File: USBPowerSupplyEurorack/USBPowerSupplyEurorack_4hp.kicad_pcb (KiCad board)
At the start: 2 copper layers, 19.9 x 110 mm, 36 parts, among them J1 1734366-1, J2 95278-501A10LF, Q1 Q_PMOS_GSD

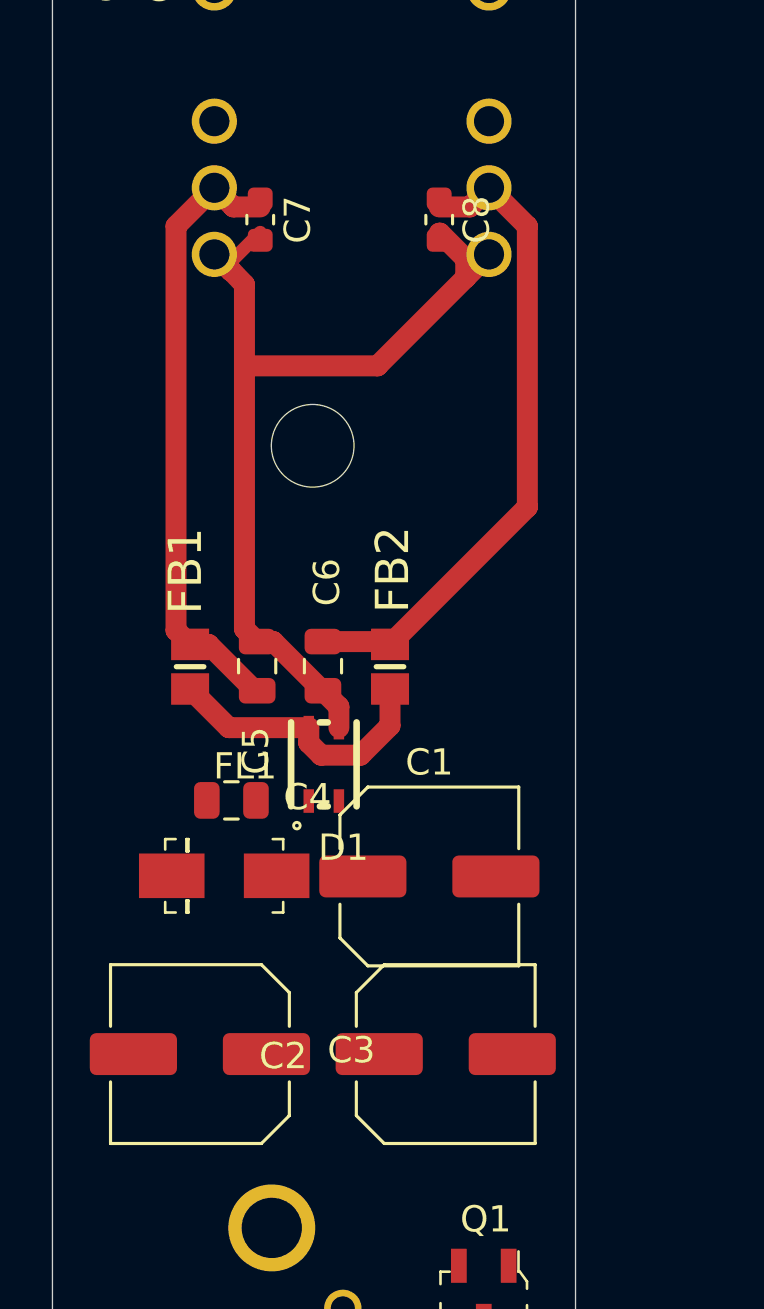
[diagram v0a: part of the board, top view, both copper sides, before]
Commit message: updated components and footprints
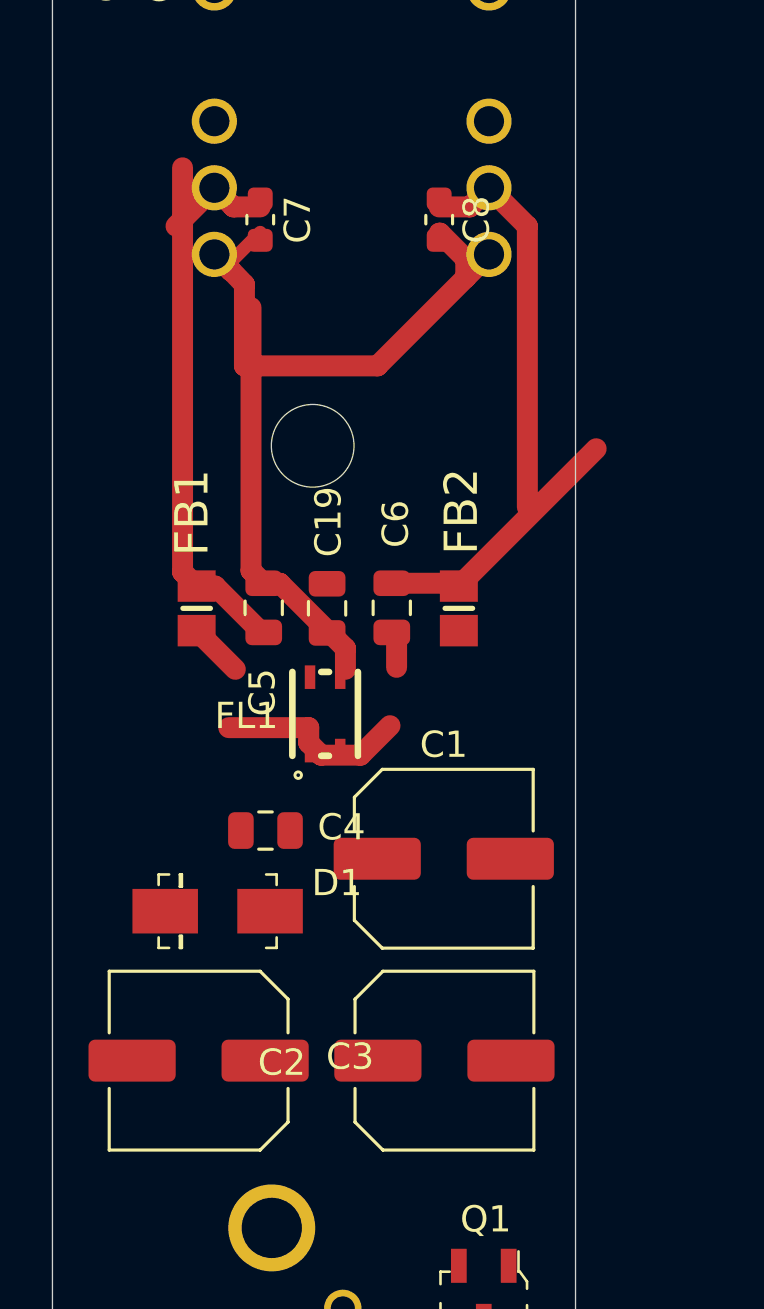
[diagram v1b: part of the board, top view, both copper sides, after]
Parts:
- added C19: 10uF, Capacitor_SMD:C_0805_2012Metric, F.Cu at (140.0, 118.8)
- moved C6 3.44 mm to (142.5, 118.7)
- moved FB2 3.44 mm to (145.1, 118.8)
- moved C5 2.24 mm to (137.6, 118.7)
- moved FB1 2.24 mm to (135.1, 118.8)
- moved FL1 1.93 mm to (139.9, 122.8)
- moved C4 1.74 mm to (137.7, 127.2)
- moved D1 1.37 mm to (135.8, 130.3)
- moved C1 0.87 mm to (144.5, 128.3)
- moved C2 0.25 mm to (144.5, 136.0)
- moved C3 0.25 mm to (135.1, 136.0)
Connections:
- FL1 pad 3: -Vin1 -> Net-(C19-Pad1)
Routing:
- net -Vin1: track 35.6 -> 37.0 mm
- net Net-(FB1-Pad2): track 10.9 -> 9.48 mm

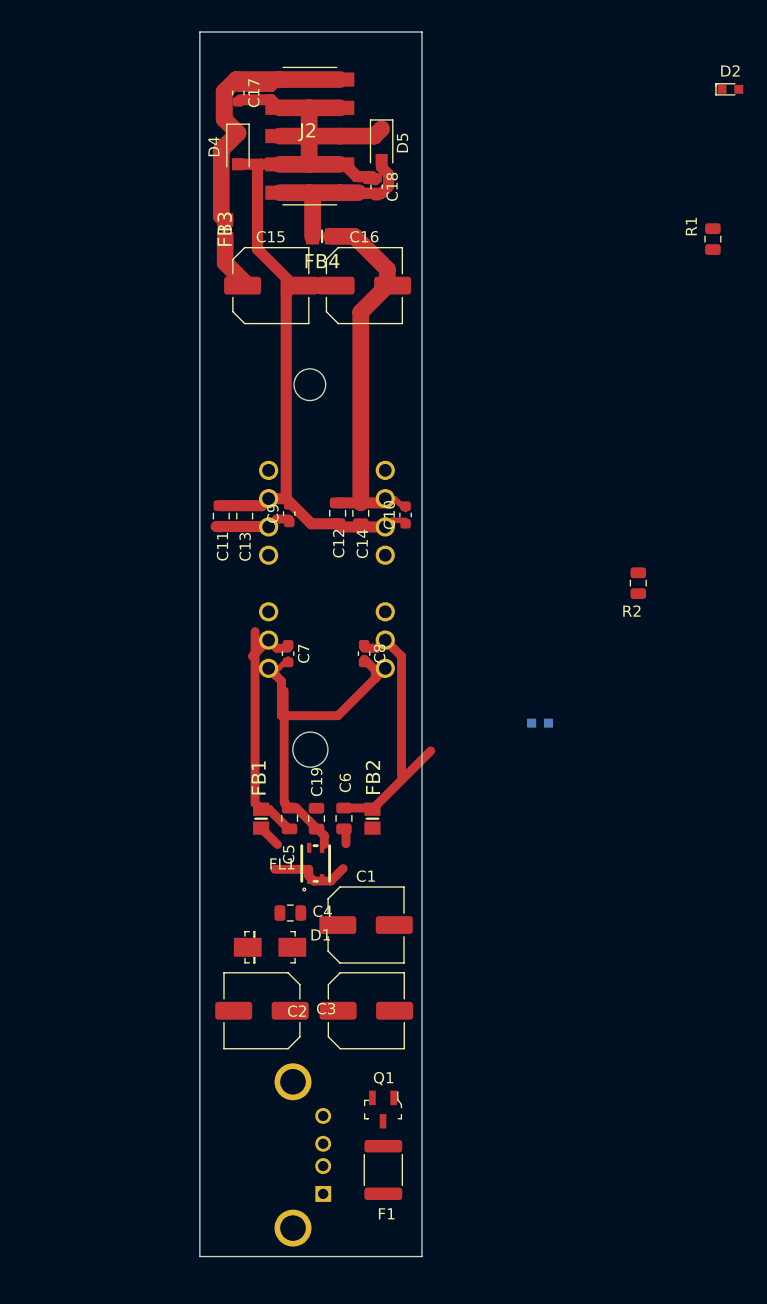
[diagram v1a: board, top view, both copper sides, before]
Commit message: moved holes for panel, updated power plug
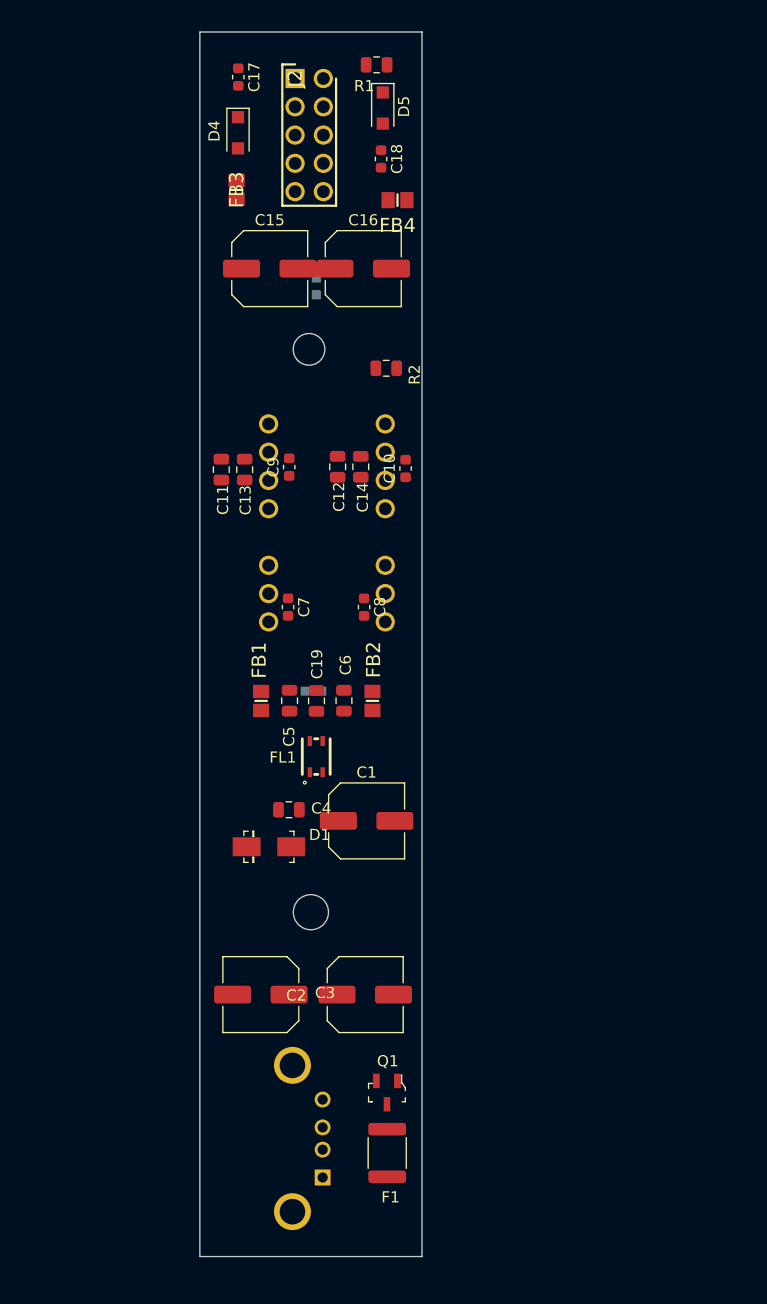
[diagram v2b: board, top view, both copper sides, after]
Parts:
- D2: moved to B.Cu
- J2: value 95278-501A10LF -> 10129381-910001BLF; footprint 95278-501A10LF:95278501A10LF -> HDRV10W67P254_2X5_1270X483X858P
- moved D2 41.2 mm to (140.0, 71.0), turned to 270 degrees
- moved R1 34.0 mm to (145.4, 51.0), turned to 180 degrees
- moved R2 29.7 mm to (146.3, 78.3), turned to 180 degrees
- moved D3 20.6 mm to (139.8, 107.3)
- moved C19 10.6 mm to (140.0, 108.2)
- moved C5 10.6 mm to (137.6, 108.2)
- moved C6 10.6 mm to (142.5, 108.2)
- moved FB1 10.6 mm to (135.1, 108.2)
- moved FB2 10.6 mm to (145.1, 108.2)
- moved FL1 9.60 mm to (140.0, 113.2)
- moved C1 9.35 mm to (144.5, 119.0)
- moved C4 9.28 mm to (137.6, 118.0)
- moved D1 9.03 mm to (135.8, 121.3)
- moved FB4 7.51 mm to (147.3, 63.2)
- moved J2 5.34 mm to (138.1, 52.3)
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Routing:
- net 0V: track 99.2 -> 0.00 mm
- net -Vin1: track 37.0 -> 0.00 mm
- net -12V: track 34.9 -> 0.00 mm
- net Net-(C17-Pad1): track 32.6 -> 0.00 mm
- net +Vin2: track 25.0 -> 0.00 mm
- net +Vin1: track 23.6 -> 0.00 mm
- net Net-(C18-Pad2): track 18.6 -> 0.00 mm
- net +12V: track 12.2 -> 0.00 mm
- net Net-(FB1-Pad2): track 9.48 -> 0.00 mm
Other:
- outline, holes or cut-outs redrawn

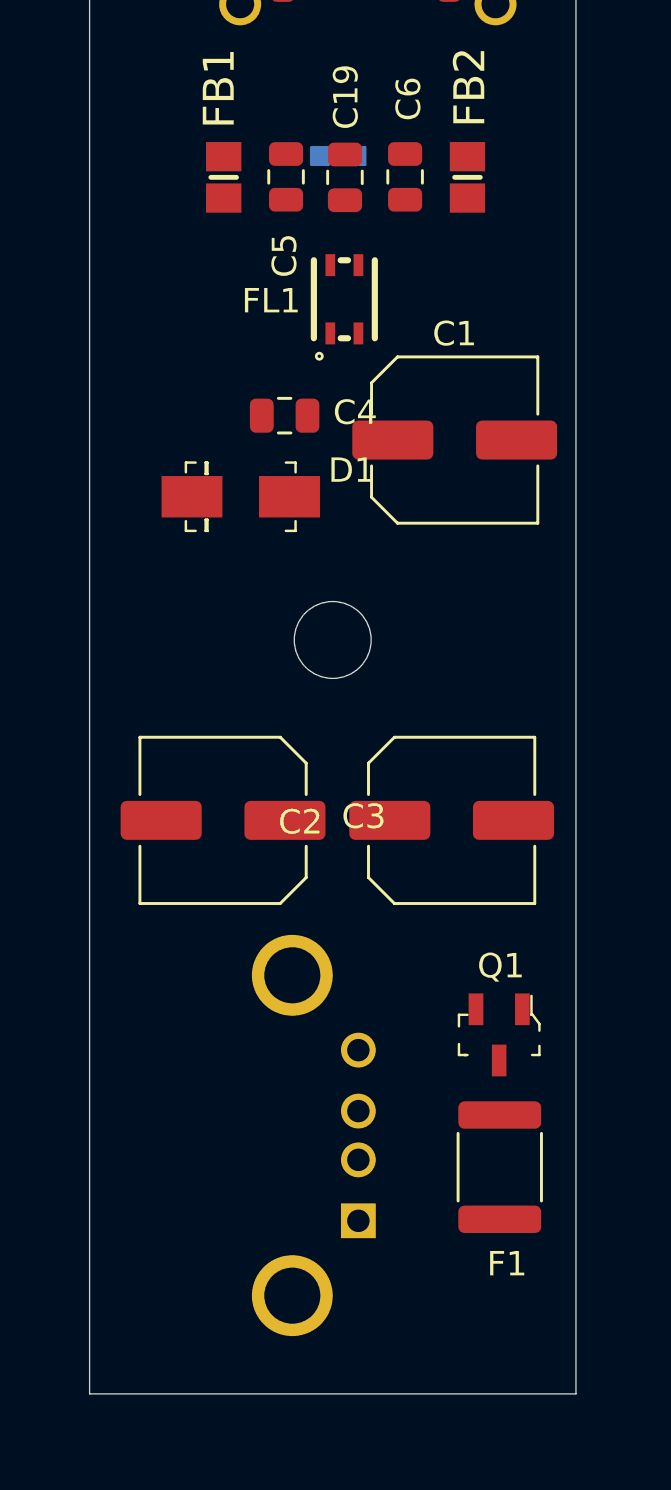
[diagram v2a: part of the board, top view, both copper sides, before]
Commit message: working on the routing, making copper pours
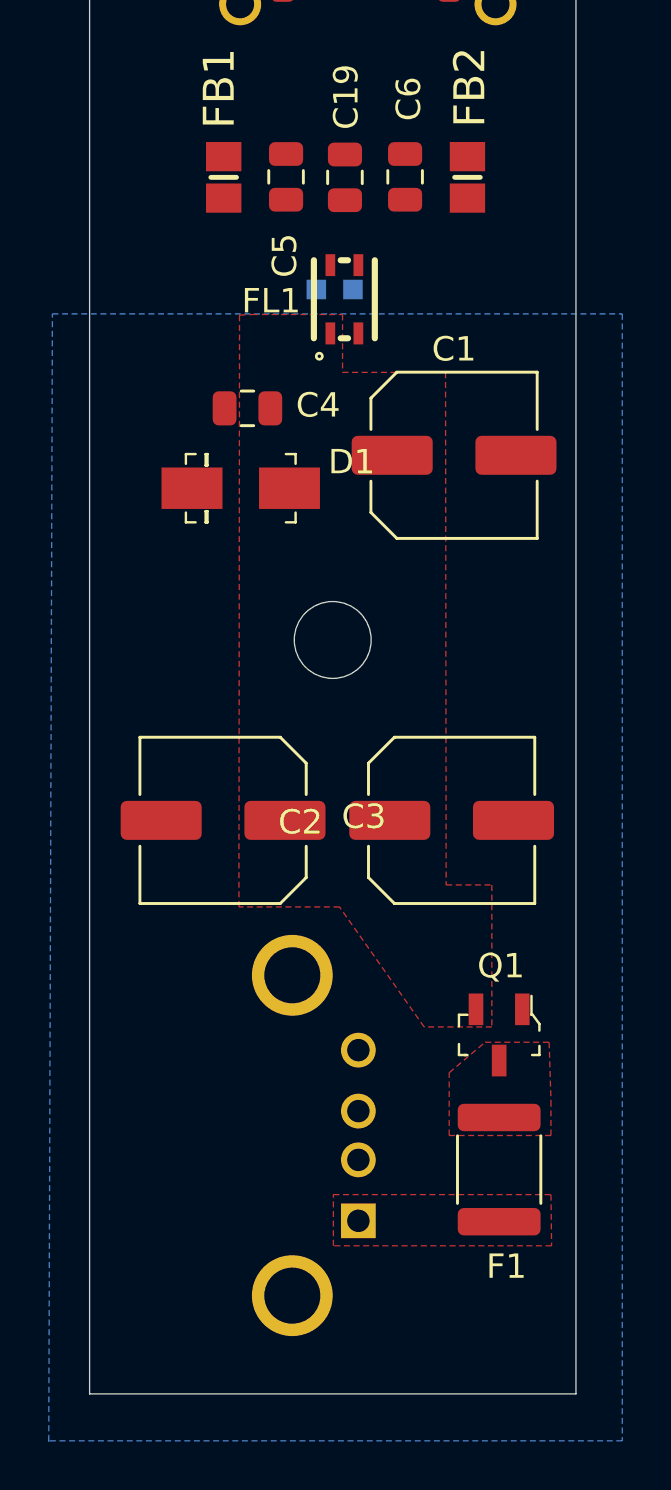
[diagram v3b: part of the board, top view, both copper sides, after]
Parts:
- moved D3 5.48 mm to (139.6, 112.8)
- moved C4 1.55 mm to (136.0, 117.7)
- moved C1 0.63 mm to (144.5, 119.6)
- moved D1 0.35 mm to (135.8, 120.9)
- moved F1 0.10 mm to (146.3, 148.9)
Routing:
- added copper zone on F.Cu, net +5V
- added copper zone on B.Cu, net GND
- added copper zone on F.Cu, net Net-(C1-Pad1)
- added copper zone on F.Cu, net Net-(F1-Pad1)

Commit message: updated readme
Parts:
- moved R1 27.7 mm to (135.5, 76.9), turned to 0 degrees
- moved C13 4.38 mm to (137.9, 87.2)
- moved C9 3.95 mm to (133.6, 87.0)
- moved C11 3.84 mm to (132.8, 83.8), turned to 0 degrees
- moved R2 3.28 mm to (144.4, 75.6), turned to 0 degrees
- moved C18 3.15 mm to (143.1, 61.1)
- moved FB4 2.80 mm to (144.6, 64.0)
- moved C17 2.71 mm to (135.3, 53.6)
- moved FB3 2.40 mm to (134.1, 64.3), turned to 180 degrees
- moved D4 2.04 mm to (134.9, 57.7), turned to 90 degrees
- moved D5 1.52 mm to (147.2, 55.8)
- moved C15 0.88 mm to (134.9, 69.4)
- moved C10 0.33 mm to (148.3, 87.1)
- moved C16 0.23 mm to (144.4, 69.3)
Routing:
- net 0V: vias 0 -> 4
- added copper zone on F.Cu, net +12V
- added copper zone on F.Cu, net -12V
- added copper zone on B.Cu, net 0V
- added copper zone on F.Cu, net 0V
- added copper zone on F.Cu, net GND

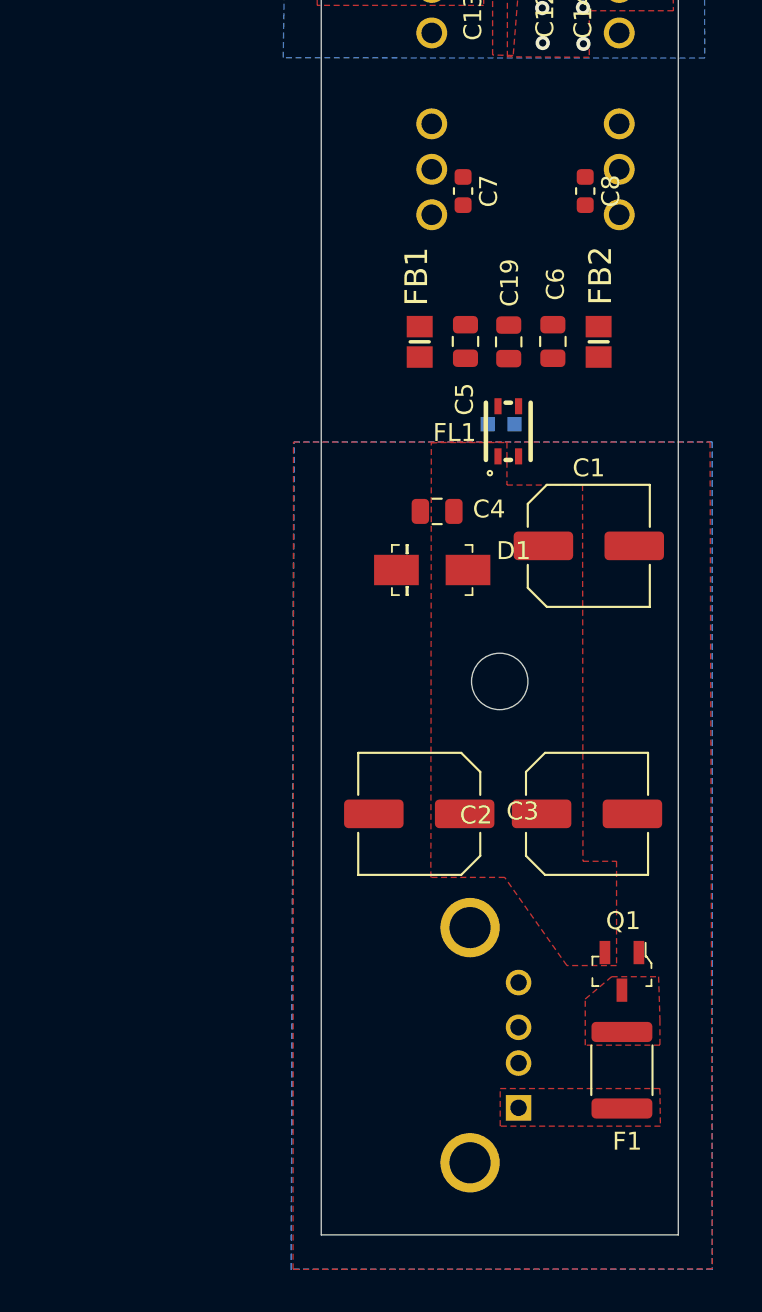
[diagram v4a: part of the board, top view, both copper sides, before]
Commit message: changed mistake in schematics
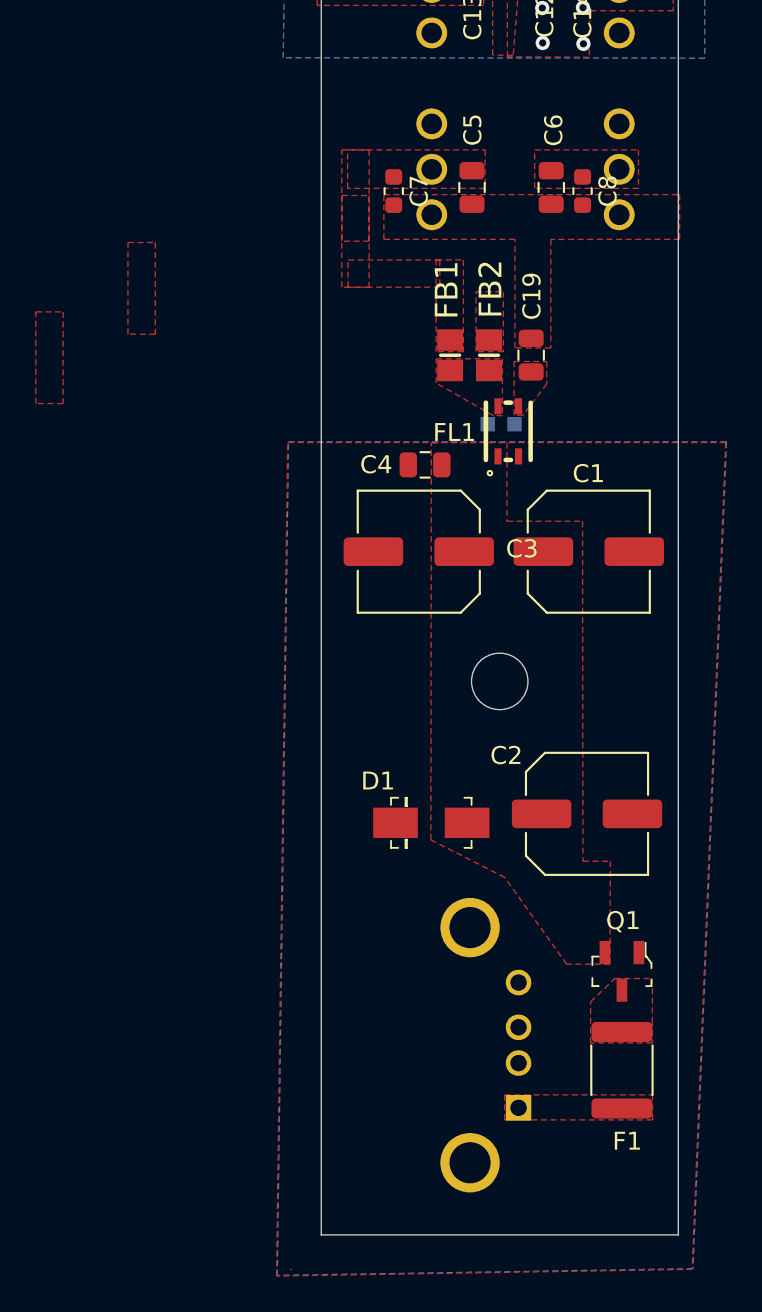
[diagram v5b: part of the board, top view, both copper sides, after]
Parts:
- moved C3 14.7 mm to (135.0, 119.9)
- moved D1 14.1 mm to (135.7, 135.1)
- moved C5 8.61 mm to (138.0, 99.5), turned to 270 degrees
- moved C6 8.61 mm to (142.4, 99.5)
- moved FB2 6.17 mm to (138.9, 108.9)
- moved C7 3.88 mm to (133.6, 99.8)
- moved C4 2.69 mm to (135.3, 115.0)
- moved FB1 1.86 mm to (136.8, 108.9)
- moved C19 1.46 mm to (141.3, 108.9)
- moved C1 0.33 mm to (144.5, 119.9)
- moved C8 0.15 mm to (144.2, 99.8)
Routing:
- added copper zone on F.Cu, net (none)
- added copper zone on F.Cu, net +Vin1
- added copper zone on F.Cu, net +Vin2
- added copper zone on F.Cu, net -Vin1
- added copper zone on F.Cu, net Net-(C19-Pad1)
- added copper zone on F.Cu, net Net-(FB1-Pad2)
